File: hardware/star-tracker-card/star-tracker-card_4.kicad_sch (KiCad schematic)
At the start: 27 parts, among them U1 RCLAMP0504FB, U7 OSD3358-512M-BSM, Y1 ECS-240-12-30BQ-AEN-TR, Y2 ABS07-32.768KHZ-T

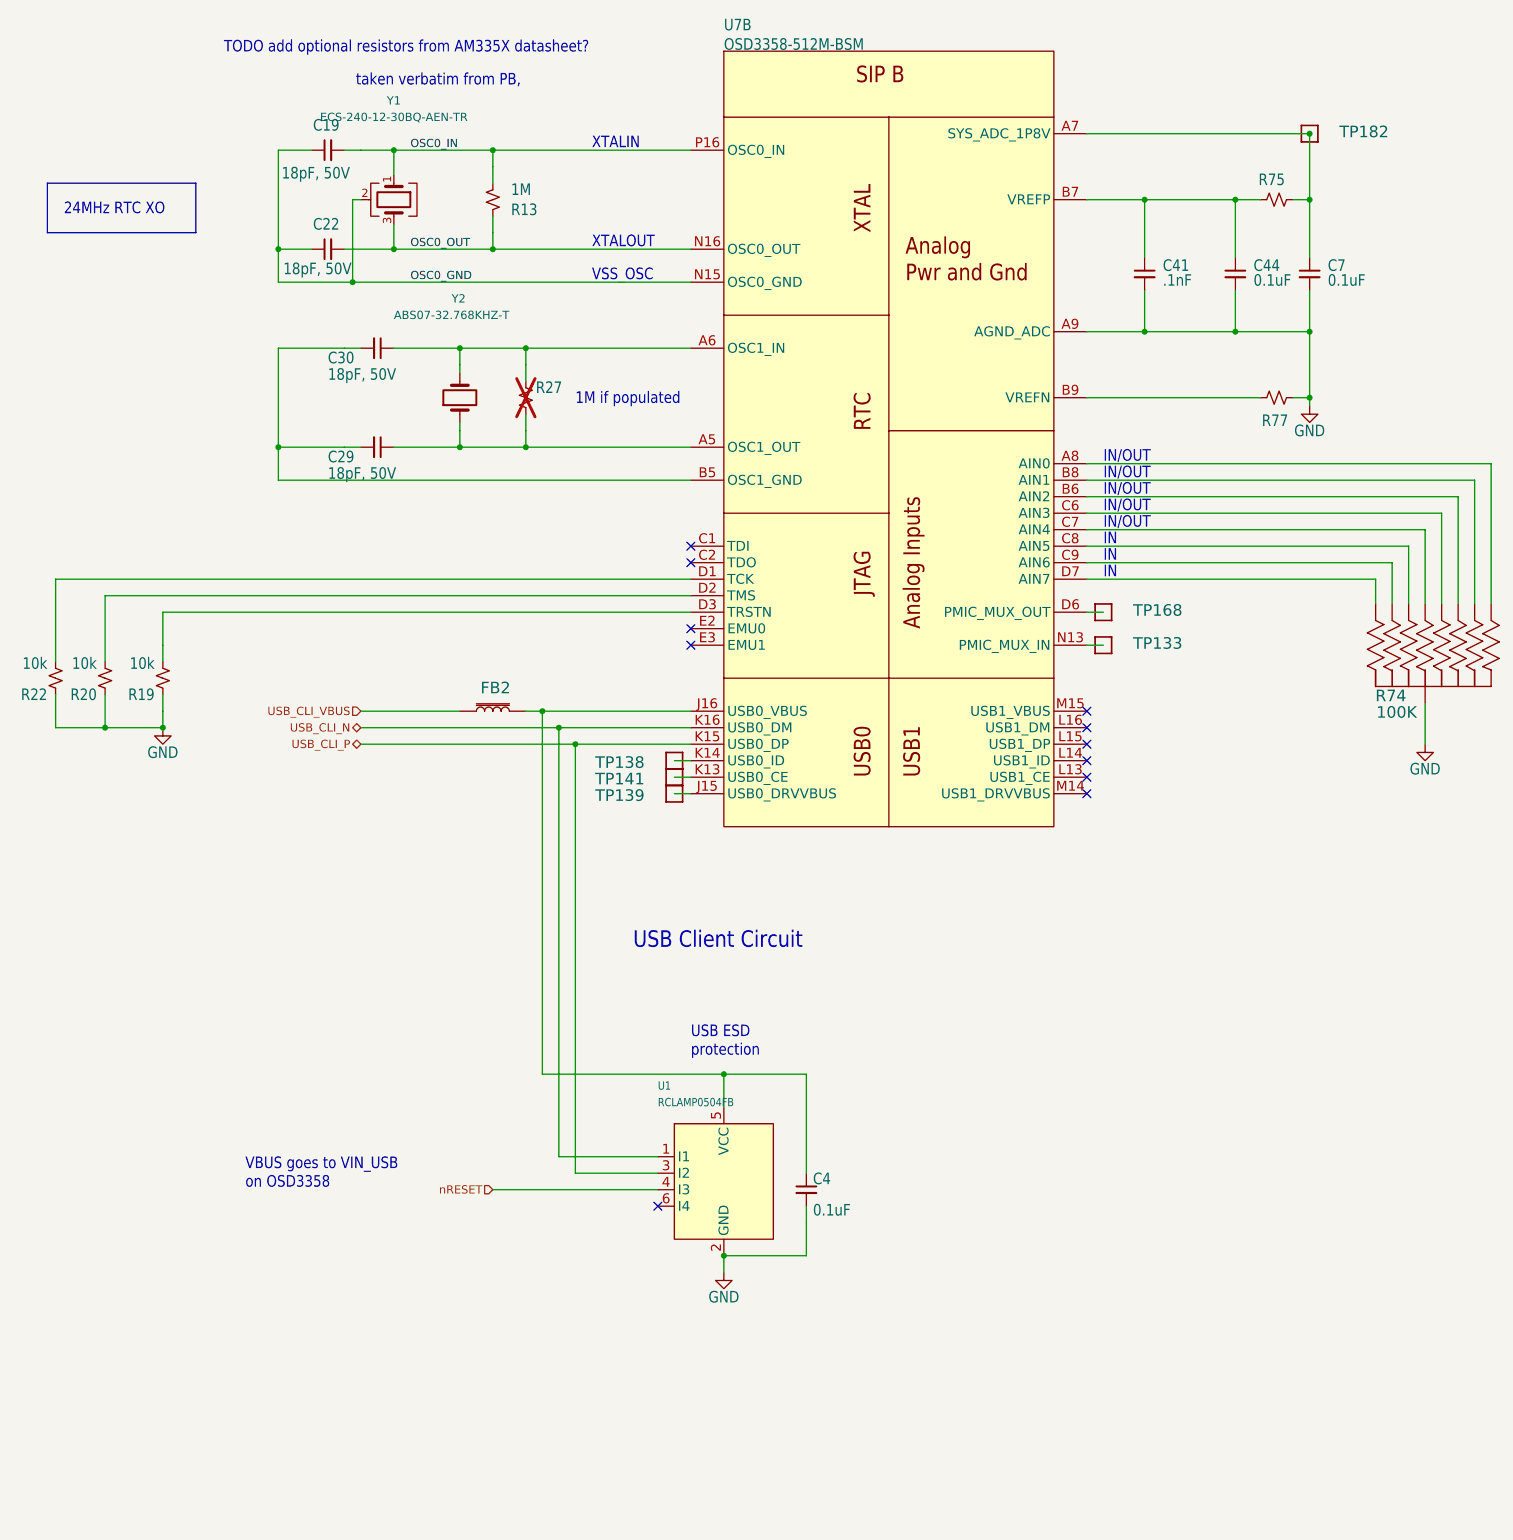
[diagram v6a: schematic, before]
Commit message: Big almost-done cleanup
Fixed a bunch of things in the schematic. Compared against C3 Octavo. Fixed all weird ERCs. Cleaned up a lot of planes on the layout. Moved uart switch, rerouted a bunch of traces for better layout. Fixed library issues, and board/sch sync issues.
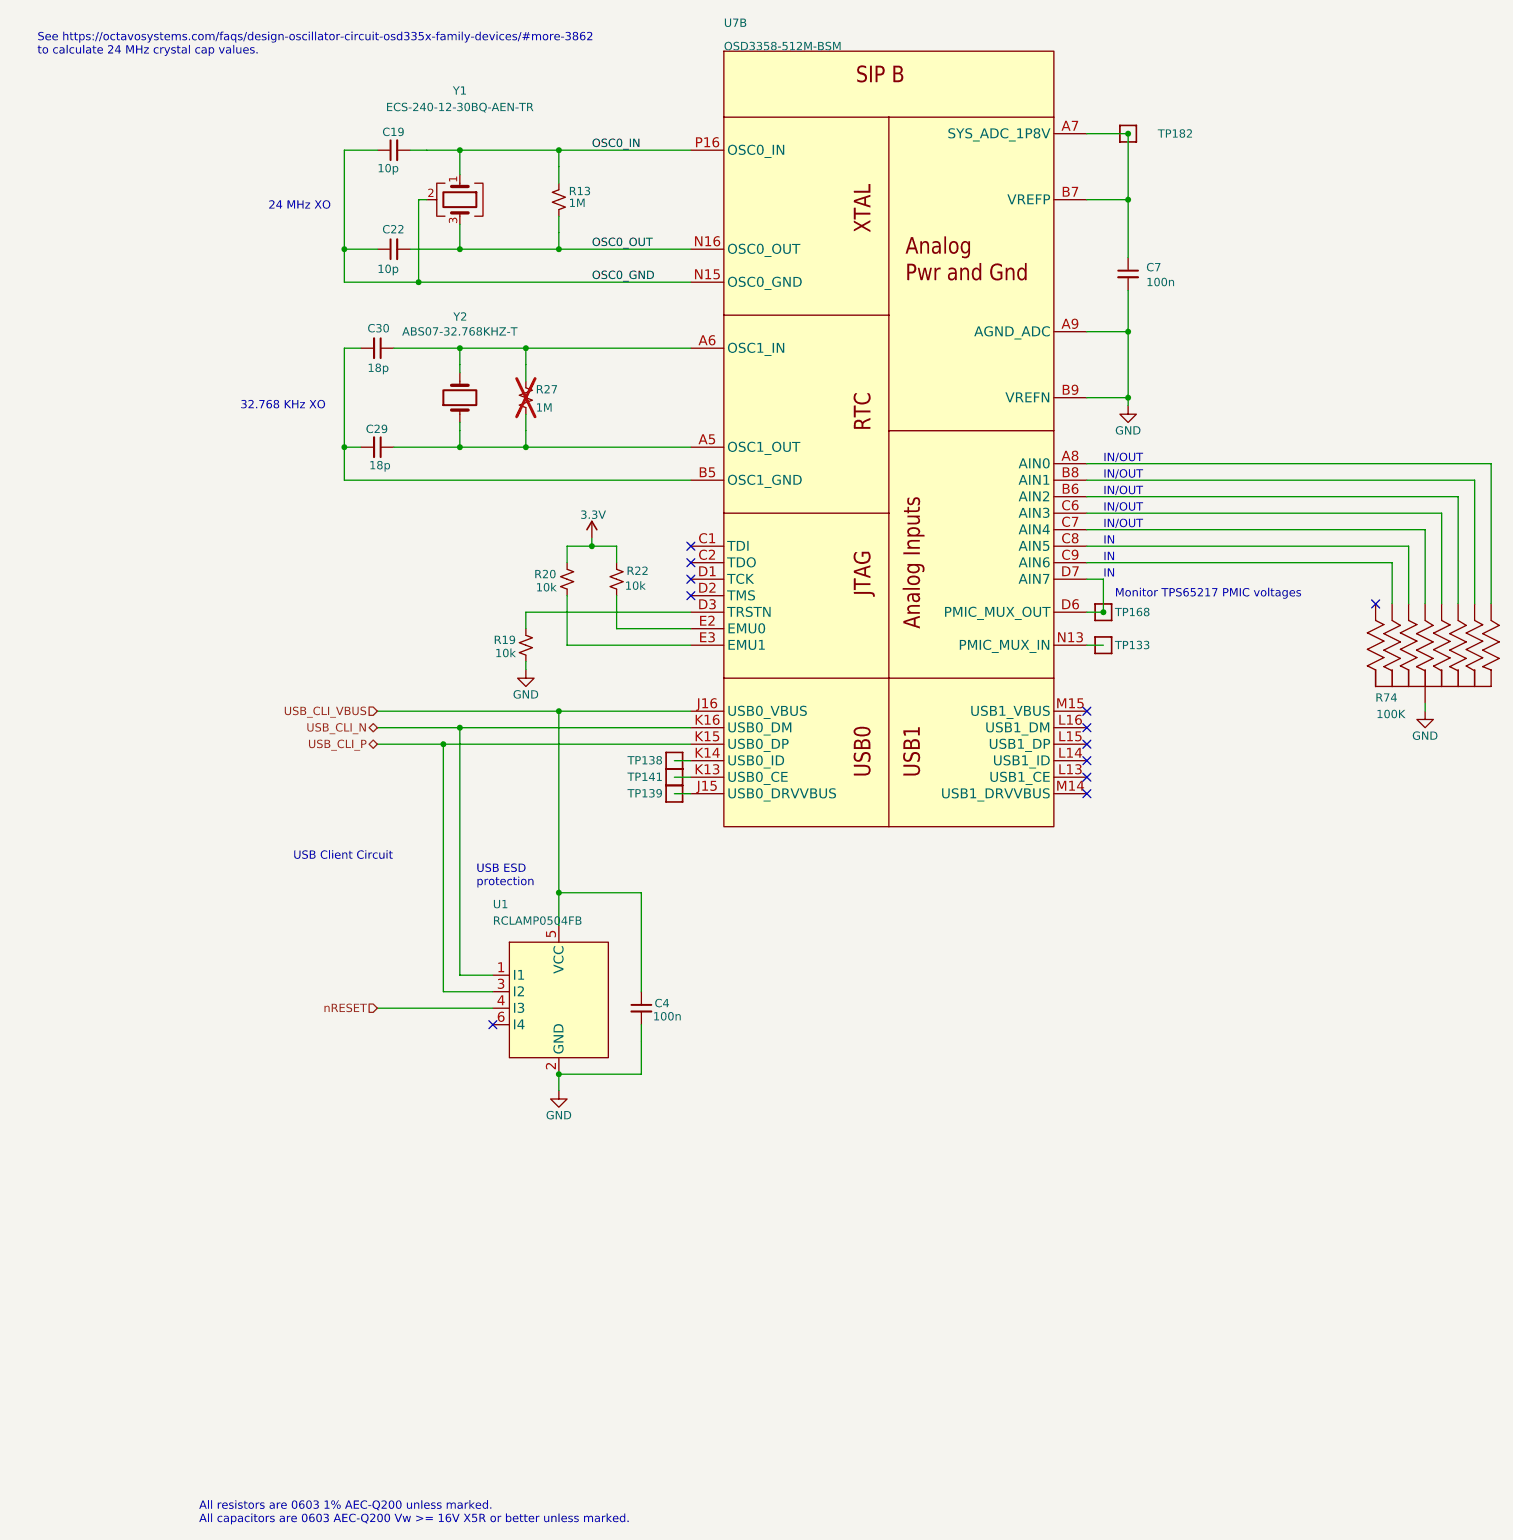
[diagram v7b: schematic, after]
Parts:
- removed C41: .1nF, oresat-passives:c_0603-SMALL, symbol Device:C_Small
- removed C44: 0.1uF, oresat-passives:c_0603-SMALL, symbol Device:C_Small
- removed FB2: 30Ω/1.8A, star-tracker-card:0603, symbol star-tracker-card-eagle-import:FERRITE_BEAD-0603
- removed R75, R77: 0, Resistor_SMD:R_0603_1608Metric, symbol Device:R_Small_US
- C19, C22: value 18pF, 50V -> 10p; footprint oresat-passives:c_0603-SMALL -> oresat-passives:0603-C-NOSILK
- C29, C30: value 18pF, 50V -> 18p; footprint oresat-passives:c_0603-SMALL -> oresat-passives:0603-C-NOSILK
- C4, C7: value 0.1uF -> 100n; footprint oresat-passives:c_0603-SMALL -> oresat-passives:0603-C-NOSILK
- R13, R19, R20, R22: footprint Resistor_SMD:R_0603_1608Metric -> oresat-passives:0603-C-NOSILK
- R27: value DNP -> 1M; footprint Resistor_SMD:R_0603_1608Metric -> oresat-passives:0603-C-NOSILK
- Y1, Y2: DST DigiKey -> (none)
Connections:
- net GND: now also U7.B9 (VREFN); no longer R20.1, R22.1
- net USB_CLI_VBUS: now also C4.1, U1.5 (VCC), U7.J16 (USB0_VBUS)
- net at TP168.1, U7.D6 (PMIC_MUX_OUT): now also U7.D7 (AIN7)
- net at U7.B7 (VREFP): now also C7.1, TP182.1, U7.A7 (SYS_ADC_1P8V)
- net at R74.6 (66): no longer U7.D7 (AIN7)
- net at R22.2: now also U7.E2 (EMU0); no longer U7.D1 (TCK)
- net at R20.2: now also U7.E3 (EMU1); no longer U7.D2 (TMS)
- new net 3.3V: R20.1, R22.1
- no-connect marks 11 -> 12
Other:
- note added: "24 MHz XO"
- note added: "32.768 KHz XO"
- note added: "All resistors are 0603 1% AEC-Q200 unless marked. All capacitors are 0603 AEC-Q200 Vw >= 16V X5R or better unless marked."
- note added: "Monitor TPS65217 PMIC voltages"
- note added: "See https://octavosystems.com/faqs/design-oscillator-circuit-osd335x-family-devices/#more-3862 to calculate 24 MHz crystal cap values."
- note removed: "1M if populated"
- note removed: "24MHz RTC XO"
- note removed: "TODO add optional resistors from AM335X datasheet?"
- note removed: "VBUS goes to VIN_USB on OSD3358"
- note removed: "VSS_OSC"
- note removed: "XTALIN"
- note removed: "XTALOUT"
- note removed: "taken verbatim from PB,"
- moved on the sheet: C19, C22, C4, C7, R13, R19, R20, R22, TP182, U1, Y1

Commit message: BOM 99% completed, push for final review
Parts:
- C19, C22: DIS (none) -> DigiKey; DPN (none) -> 399-16015-1-ND; MFR (none) -> KEMET; MPN (none) -> C0603C100J1GACAUTO
- C29, C30: DIS (none) -> DigiKey; DPN (none) -> 399-15781-1-ND; MFR (none) -> KEMET; MPN (none) -> C0603C180J1GACAUTO
- C4, C7: DIS (none) -> DigiKey; DPN (none) -> 399-6856-1-ND; MFR (none) -> KEMET; MPN (none) -> C0603C104K5RACAUTO
- R13: DIS (none) -> DigiKey; DPN (none) -> RMCF0603FT1M00CT-ND; MFR (none) -> Stackpole Electronics; MPN (none) -> RMCF0603FT1M00
- R19, R20, R22: DIS (none) -> DigiKey; DPN (none) -> RMCF0603FT10K0CT-ND; MFR (none) -> Stackpole Electronics; MPN (none) -> RMCF0603FT10K0
- R74: DIS (none) -> DigiKey; MFR (none) -> Panasonic Industry
- U1: DIS (none) -> DigiKey; DPN (none) -> RCLAMP0504FBTCTCT-ND; MFR (none) -> Semtech Corporation; MPN (none) -> RCLAMP0504FBTCT
- U7: DIS (none) -> DigiKey; DPN (none) -> 1676-OSD3358-1G-ISM-ND; MFR (none) -> Octavo Systems LLC; MPN (none) -> OSD3358-1G-ISM
